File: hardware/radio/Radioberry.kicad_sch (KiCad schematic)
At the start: 4 parts

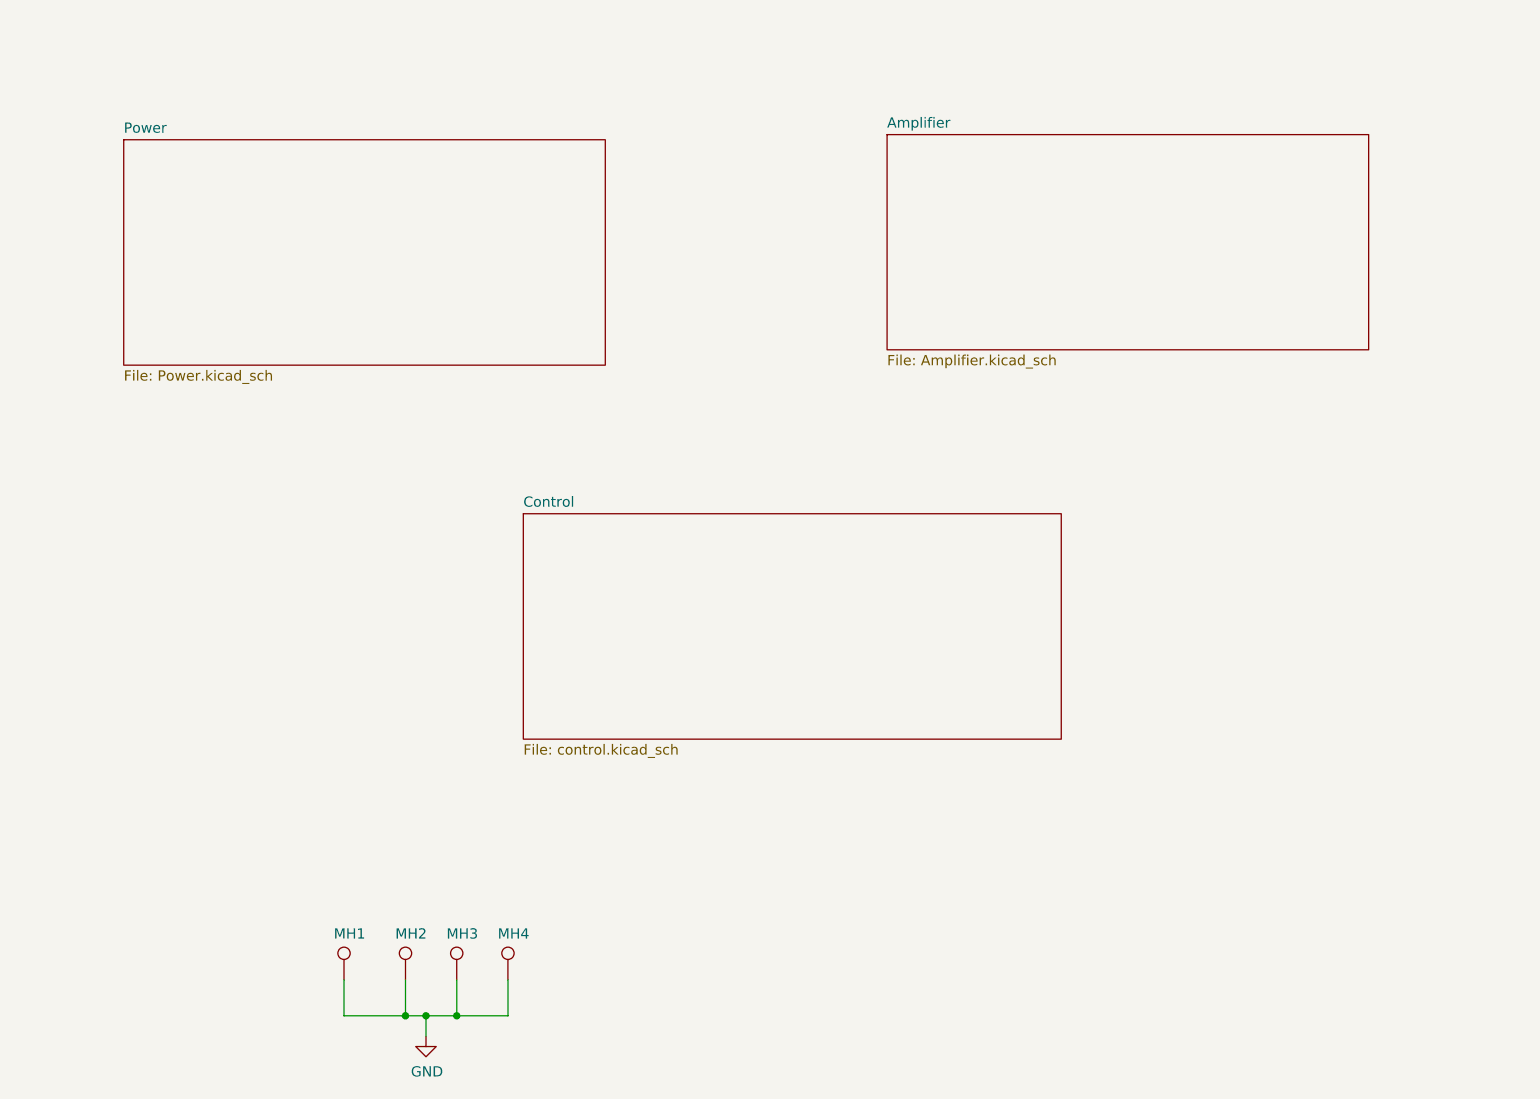
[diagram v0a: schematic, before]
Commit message: kicad 8.0 conversion
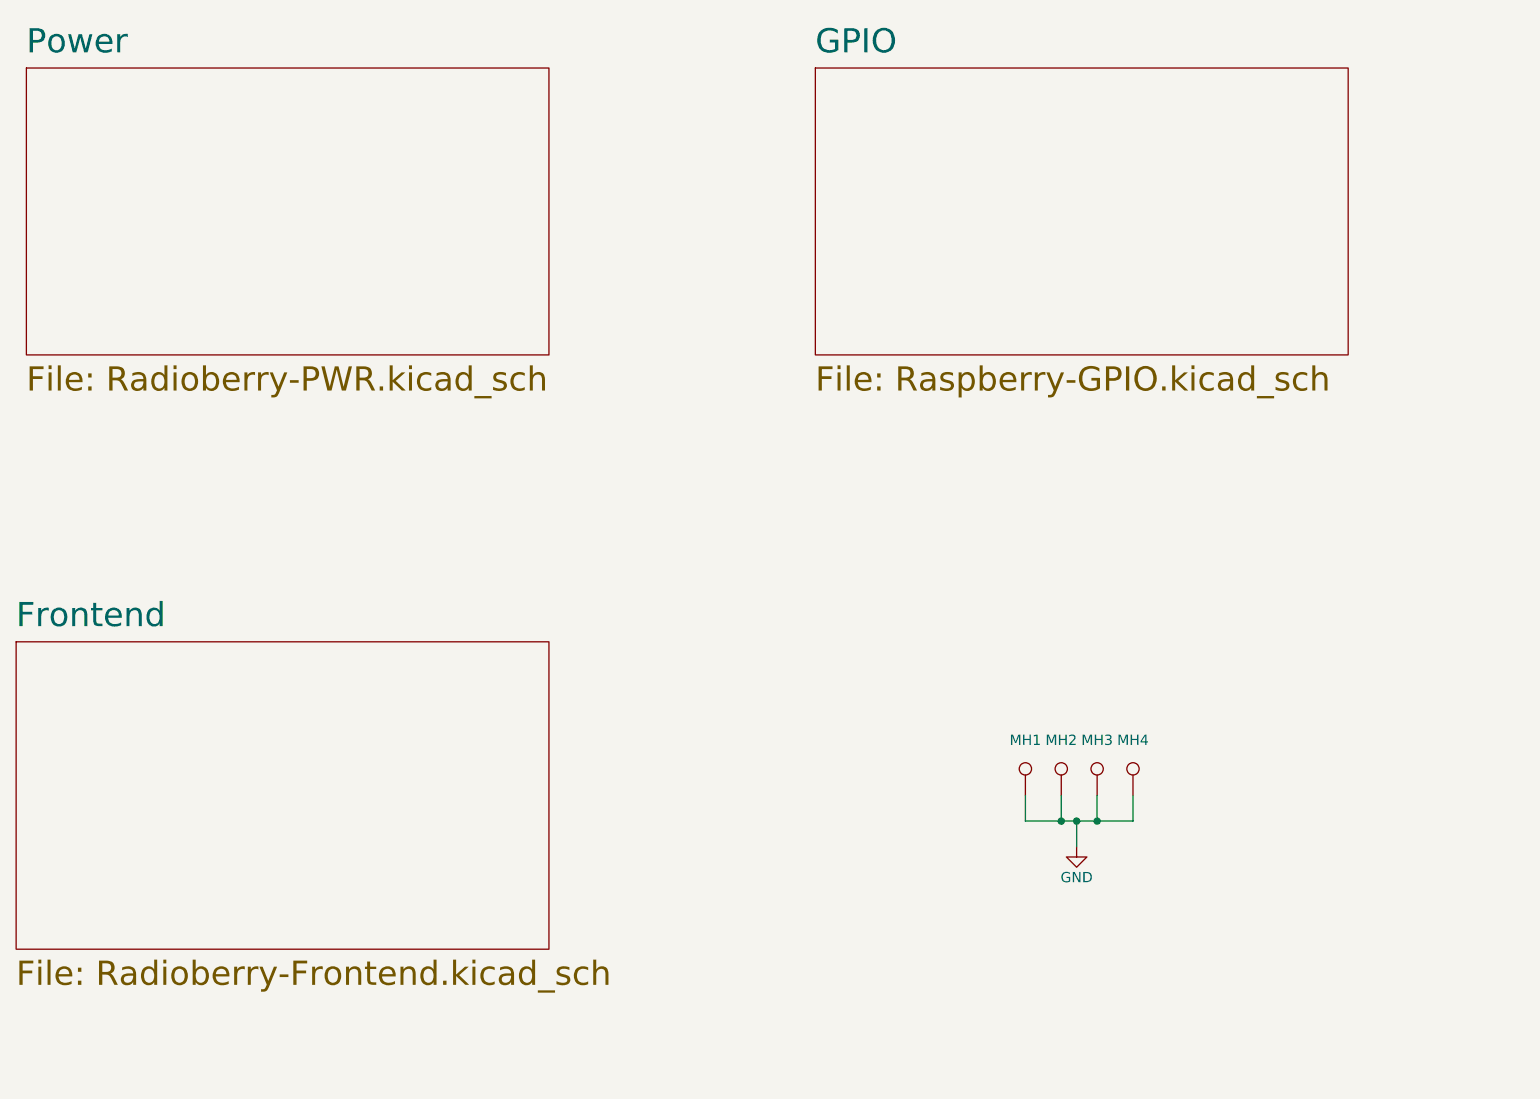
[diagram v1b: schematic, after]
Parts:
- MH1, MH4: footprint HERMESLITE:m3 -> hermeslite:m3; Option DNI -> DUMMY
- MH2, MH3: footprint HERMESLITE:m3 -> hermeslite:m3; Option (none) -> DUMMY; Option  DNI -> (none)
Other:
- removed sheet Amplifier
- removed sheet Control
- added sheet Frontend (Radioberry-Frontend.kicad_sch)
- added sheet GPIO (Raspberry-GPIO.kicad_sch)
- sheet Power: file Power.kicad_sch -> Radioberry-PWR.kicad_sch
- title: Radioberry - amplifier -> RadioBerry V2.0
